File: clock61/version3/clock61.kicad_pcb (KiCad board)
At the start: 2 copper layers, 55.2 x 55.2 mm, 82 parts

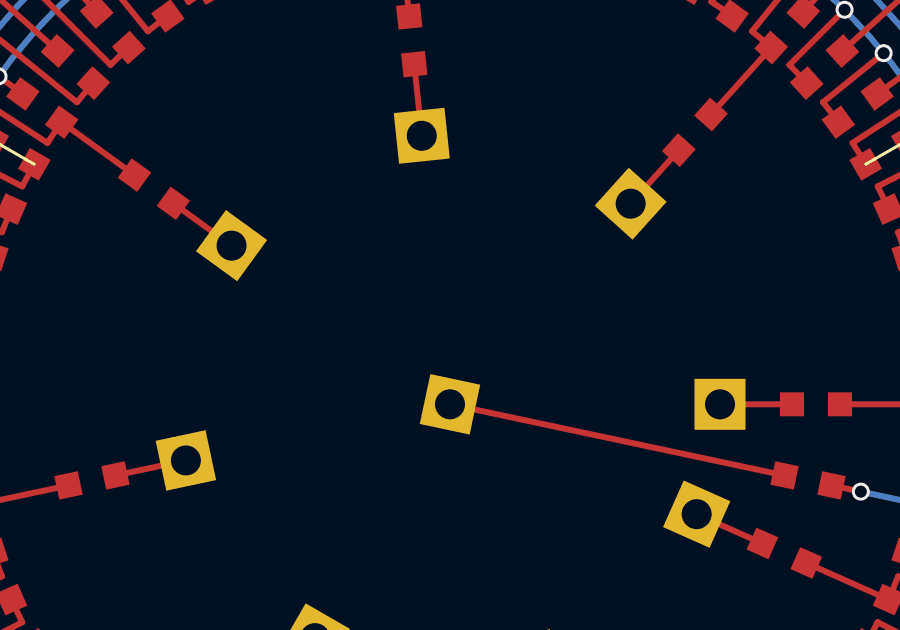
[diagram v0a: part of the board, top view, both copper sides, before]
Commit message: subtle changes to make a kicad version 3 file so more folks can view it
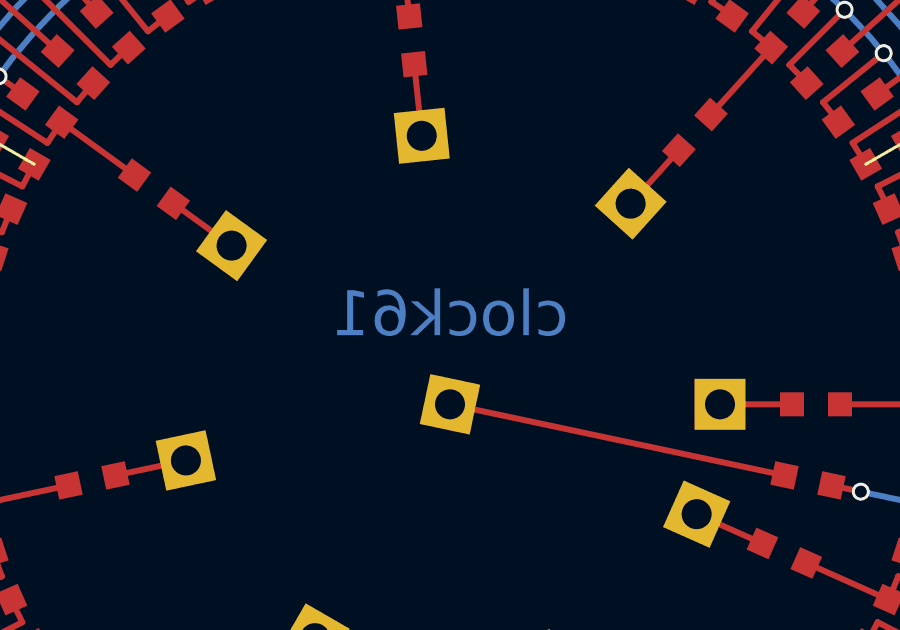
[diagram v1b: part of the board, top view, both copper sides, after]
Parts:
- removed the ? at (150.0, 100.0) (x69)
- added ? (x60): , min:hand, F.Cu at (150.0, 100.0)
- added ? (x9): , resi:stor, F.Cu at (150.0, 100.0)
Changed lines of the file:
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@@
     (pad 1 thru_hole circle (at 0 0) (size 3 3) (drill 3) (layers *.Cu *.Mask F.SilkS))
   )
-(gr_text clock61 (at 150  97) (layer B.SilkS) (effects (font (size 1.5 1.5) (thickness 0.3))(justify mirror)) )
+(gr_text clock61 (at 150  97) (layer B.Cu) (effects (font (size 1.5 1.5) (thickness 0.3))(justify mirror)) )
 )
